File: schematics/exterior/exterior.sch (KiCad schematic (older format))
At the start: 71 parts

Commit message: separated the interior and exterior schematics
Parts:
- removed DOOR_LOCK_STRIKE: L, symbol Device:L
- removed J?: RJ45, symbol Connector:RJ45
- removed Q?: TIP120, Package_TO_SOT_THT:TO-220-3_Vertical, symbol Transistor_BJT:TIP120
- removed R?: 330, symbol Device:R
- removed R? (x4): 1K, symbol Device:R
- removed U?: MAX489E, symbol Interface_UART:MAX489E
- removed U?: VX7805, symbol Regulator_Linear:L7805
- gave numbers to parts that had none: 1
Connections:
- net labels removed: 12V, BCM_14, BCM_15, BCM_18
- wire segments 207 -> 161
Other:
- note added: "…. 16 total"
- note removed: "ALL BCM IN INTERIOR\nGO TO RPI0W\n"
- note removed: "INTERIOR"
- note removed: "MAINS PSU\nRS-25-12"
- note removed: "TO MAINS"
- note removed: "…. 12 total"

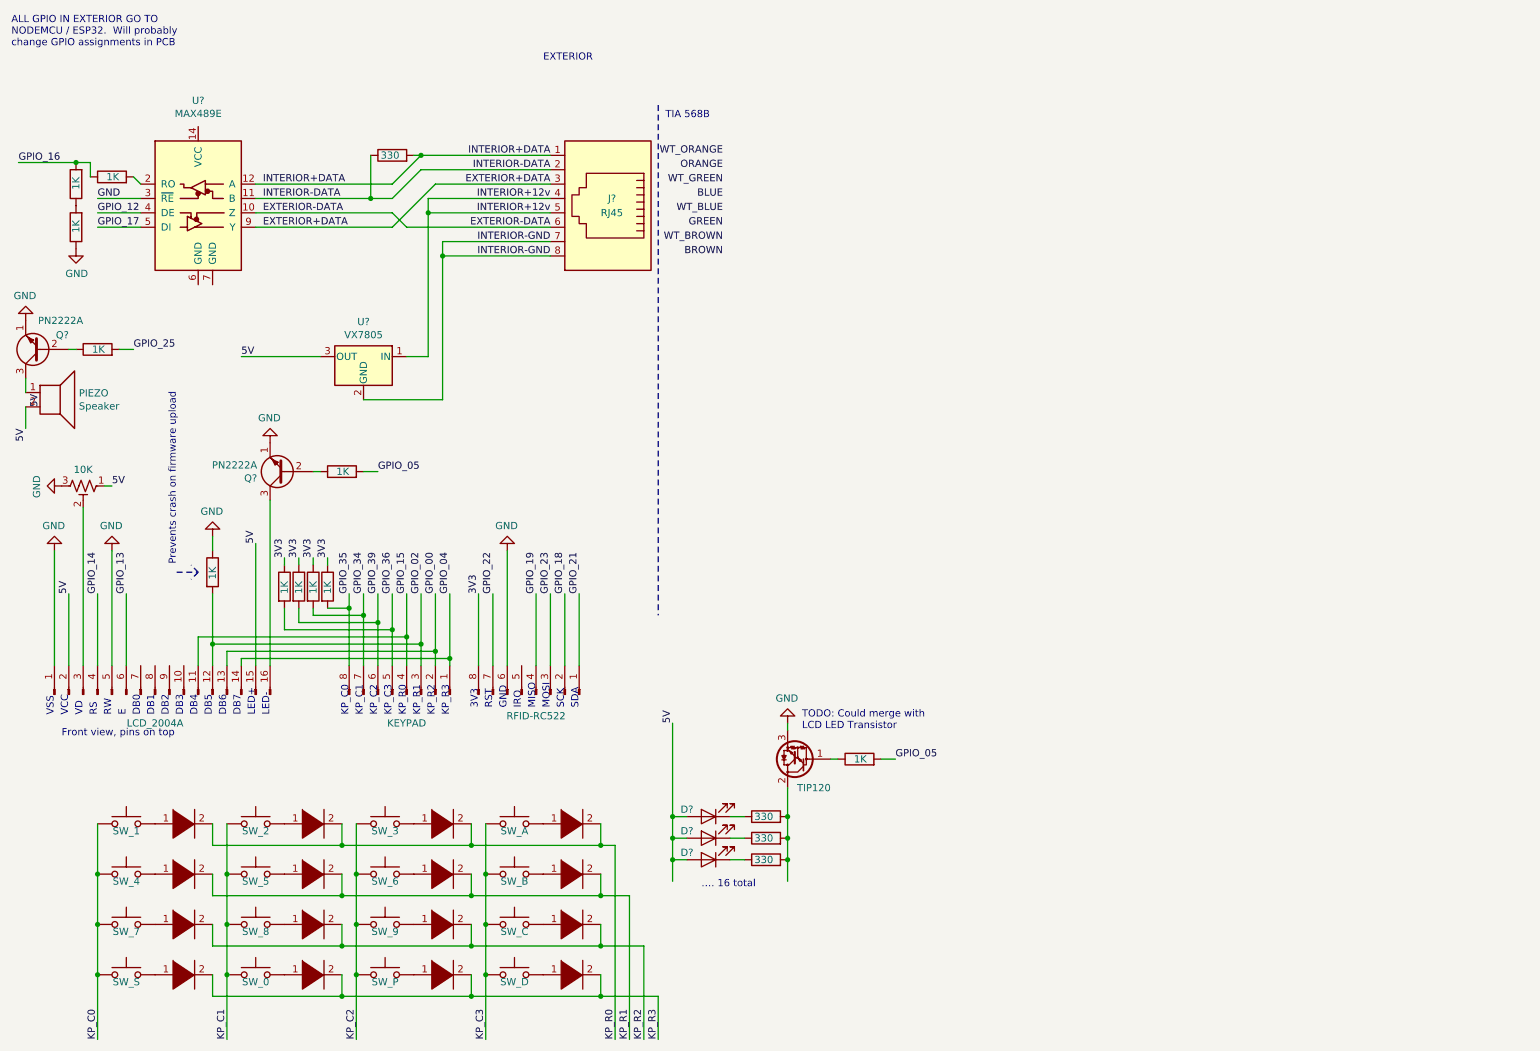
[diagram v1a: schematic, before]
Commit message: Reworked keypad so that it has connectors
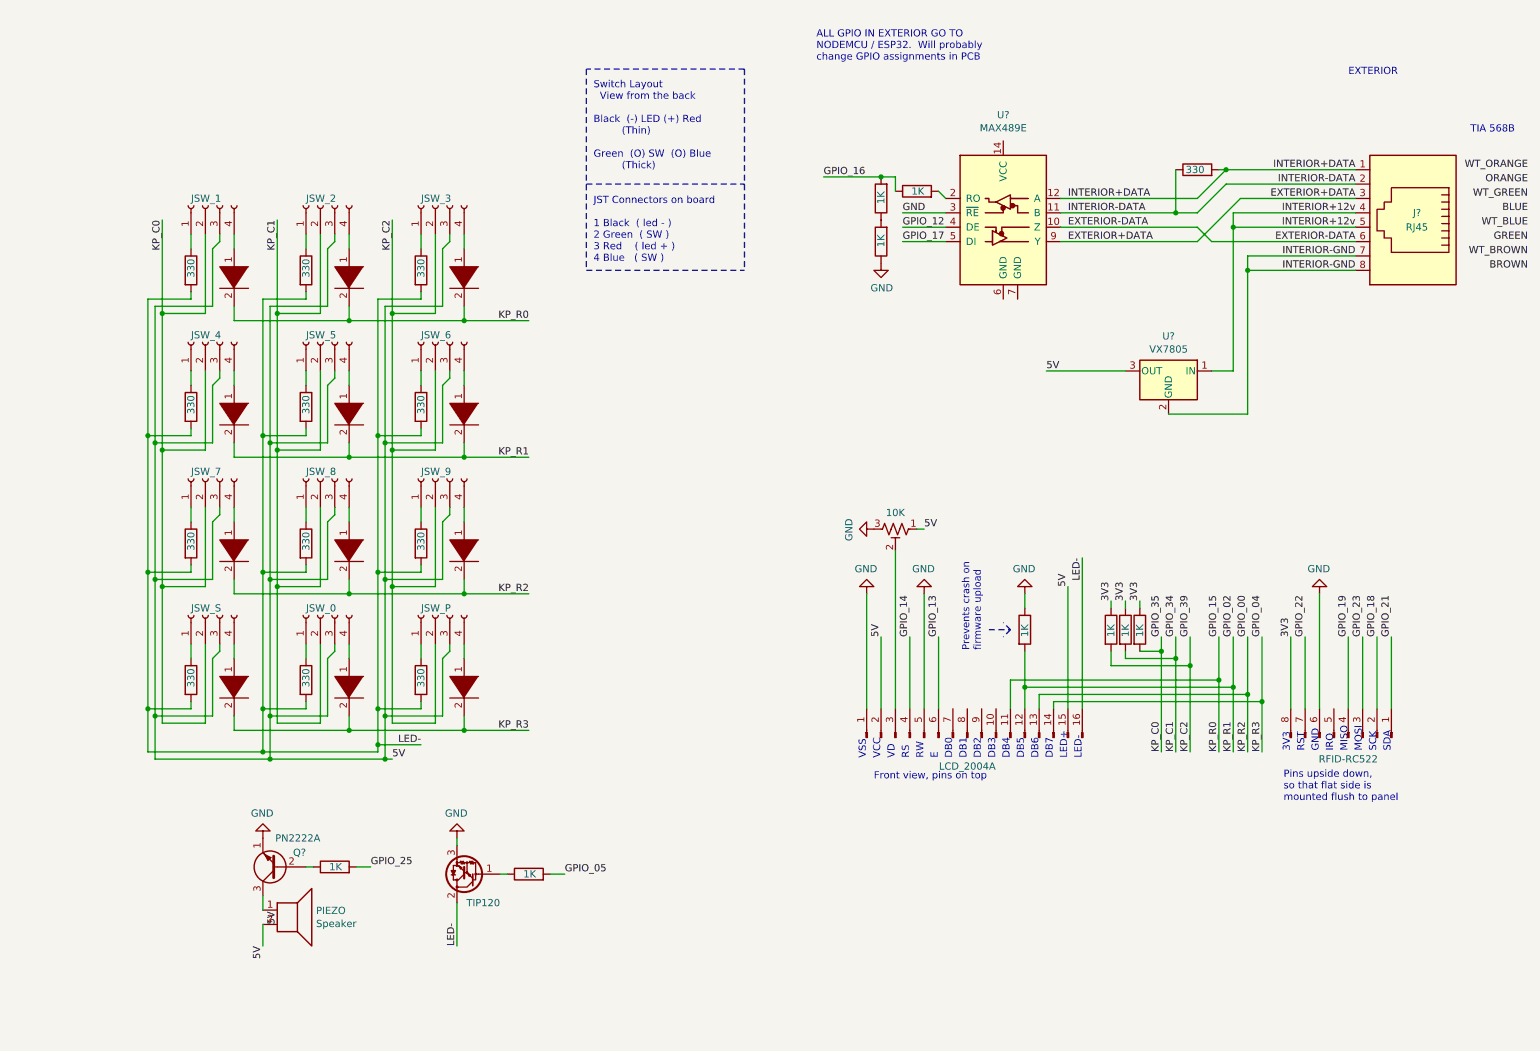
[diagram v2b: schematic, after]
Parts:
- removed D? (x16): DIODE, symbol pspice:DIODE
- removed D? (x3): LED, symbol Device:LED
- removed J?: KEYPAD, symbol Connector:Conn_01x08_Male
- removed Q?: PN2222A, Package_TO_SOT_THT:TO-92_Inline, symbol Transistor_BJT:PN2222A
- removed Q?: TIP120, Package_TO_SOT_THT:TO-220-3_Vertical, symbol Transistor_BJT:TIP120
- removed R? (x3): 1K, symbol Device:R
- removed R? (x3): 330, symbol Device:R
- removed SW_0, SW_1, SW_2, SW_3, SW_4, SW_5, SW_6, SW_7, SW_8, SW_9, SW_A, SW_B, SW_C, SW_D, SW_P, SW_S: SW_SPST, symbol Switch:SW_Push
- added D? (x12): DIODE, symbol pspice:DIODE
- added JSW_0, JSW_1, JSW_2, JSW_3, JSW_4, JSW_5, JSW_6, JSW_7, JSW_8, JSW_9, JSW_P, JSW_S: Conn_01x04_Female, symbol Connector:Conn_01x04_Female
- added Q?: TIP120, Package_TO_SOT_THT:TO-220-3_Vertical, symbol Transistor_BJT:TIP120
- added R? (x12): 330, symbol Device:R
- added R?: 1K, symbol Device:R
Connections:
- net 5V: now also JSW_0.3 (Pin_3), JSW_1.3 (Pin_3), JSW_2.3 (Pin_3), JSW_3.3 (Pin_3), JSW_4.3 (Pin_3), JSW_5.3 (Pin_3), JSW_6.3 (Pin_3), JSW_7.3 (Pin_3), JSW_8.3 (Pin_3), JSW_9.3 (Pin_3), JSW_P.3 (Pin_3), JSW_S.3 (Pin_3)
- net GND: now also Q?.3 (E)
- net GPIO_00: now also D?.2 (A), D?.2 (A), D?.2 (A)
- net GPIO_02: now also D?.2 (A), D?.2 (A), D?.2 (A)
- net GPIO_04: now also D?.2 (A), D?.2 (A), D?.2 (A)
- net GPIO_05: now also R?.2
- net GPIO_15: now also D?.2 (A), D?.2 (A), D?.2 (A)
- net GPIO_34: now also JSW_0.2 (Pin_2), JSW_2.2 (Pin_2), JSW_5.2 (Pin_2), JSW_8.2 (Pin_2)
- net GPIO_35: now also JSW_1.2 (Pin_2), JSW_4.2 (Pin_2), JSW_7.2 (Pin_2), JSW_S.2 (Pin_2)
- net GPIO_39: now also JSW_3.2 (Pin_2), JSW_6.2 (Pin_2), JSW_9.2 (Pin_2), JSW_P.2 (Pin_2)
- net LED-: now reaches LCD_2004A.16 (Pin_16)
- net LED-: now also Q?.2 (C), R?.2, R?.2, R?.2, R?.2, R?.2, R?.2, R?.2, R?.2, R?.2, R?.2, R?.2, R?.2
- new net: JSW_1.1 (Pin_1), R?.1
- new net: D?.1 (K), JSW_1.4 (Pin_4)
- new net: JSW_2.1 (Pin_1), R?.1
- new net: D?.1 (K), JSW_2.4 (Pin_4)
- new net: JSW_3.1 (Pin_1), R?.1
- new net: D?.1 (K), JSW_3.4 (Pin_4)
- new net: JSW_4.1 (Pin_1), R?.1
- new net: D?.1 (K), JSW_4.4 (Pin_4)
- new net: JSW_5.1 (Pin_1), R?.1
- new net: D?.1 (K), JSW_5.4 (Pin_4)
- new net: JSW_6.1 (Pin_1), R?.1
- new net: D?.1 (K), JSW_6.4 (Pin_4)
- new net: JSW_7.1 (Pin_1), R?.1
- new net: D?.1 (K), JSW_7.4 (Pin_4)
- new net: JSW_8.1 (Pin_1), R?.1
- new net: D?.1 (K), JSW_8.4 (Pin_4)
- new net: JSW_9.1 (Pin_1), R?.1
- new net: D?.1 (K), JSW_9.4 (Pin_4)
- new net: JSW_S.1 (Pin_1), R?.1
- new net: D?.1 (K), JSW_S.4 (Pin_4)
- new net: JSW_0.1 (Pin_1), R?.1
- new net: D?.1 (K), JSW_0.4 (Pin_4)
- new net: JSW_P.1 (Pin_1), R?.1
- new net: D?.1 (K), JSW_P.4 (Pin_4)
- new net: Q?.1 (B), R?.1
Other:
- note added: "Pins upside down,\nso that flat side is\nmounted flush to panel"
- note added: "Prevents crash on\nfirmware upload"
- note added: "Switch Layout\n View from the back\n\nBlack (-) LED (+) Red\n (Thin)\n\nGreen (O) SW (O) Blue\n (Thick)\n\n\nJST Connectors on board\n\n1 Black ( led - )\n2 Green ( SW )\n3 Red ( led + )\n4 Blue ( SW )\n"
- note removed: "KP_C0"
- note removed: "KP_C1"
- note removed: "KP_C2"
- note removed: "KP_C3"
- note removed: "KP_R0"
- note removed: "KP_R1"
- note removed: "KP_R2"
- note removed: "KP_R3"
- note removed: "Prevents crash on firmware upload"
- note removed: "TODO: Could merge with \nLCD LED Transistor\n"
- note removed: "…. 16 total"
- moved on the sheet: J?, LCD_2004A, PIEZO, Q?, U?
